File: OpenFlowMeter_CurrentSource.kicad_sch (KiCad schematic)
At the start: 21 parts, among them J1 Screw_Terminal_01x02, Q1 BC856, U1 LT1492

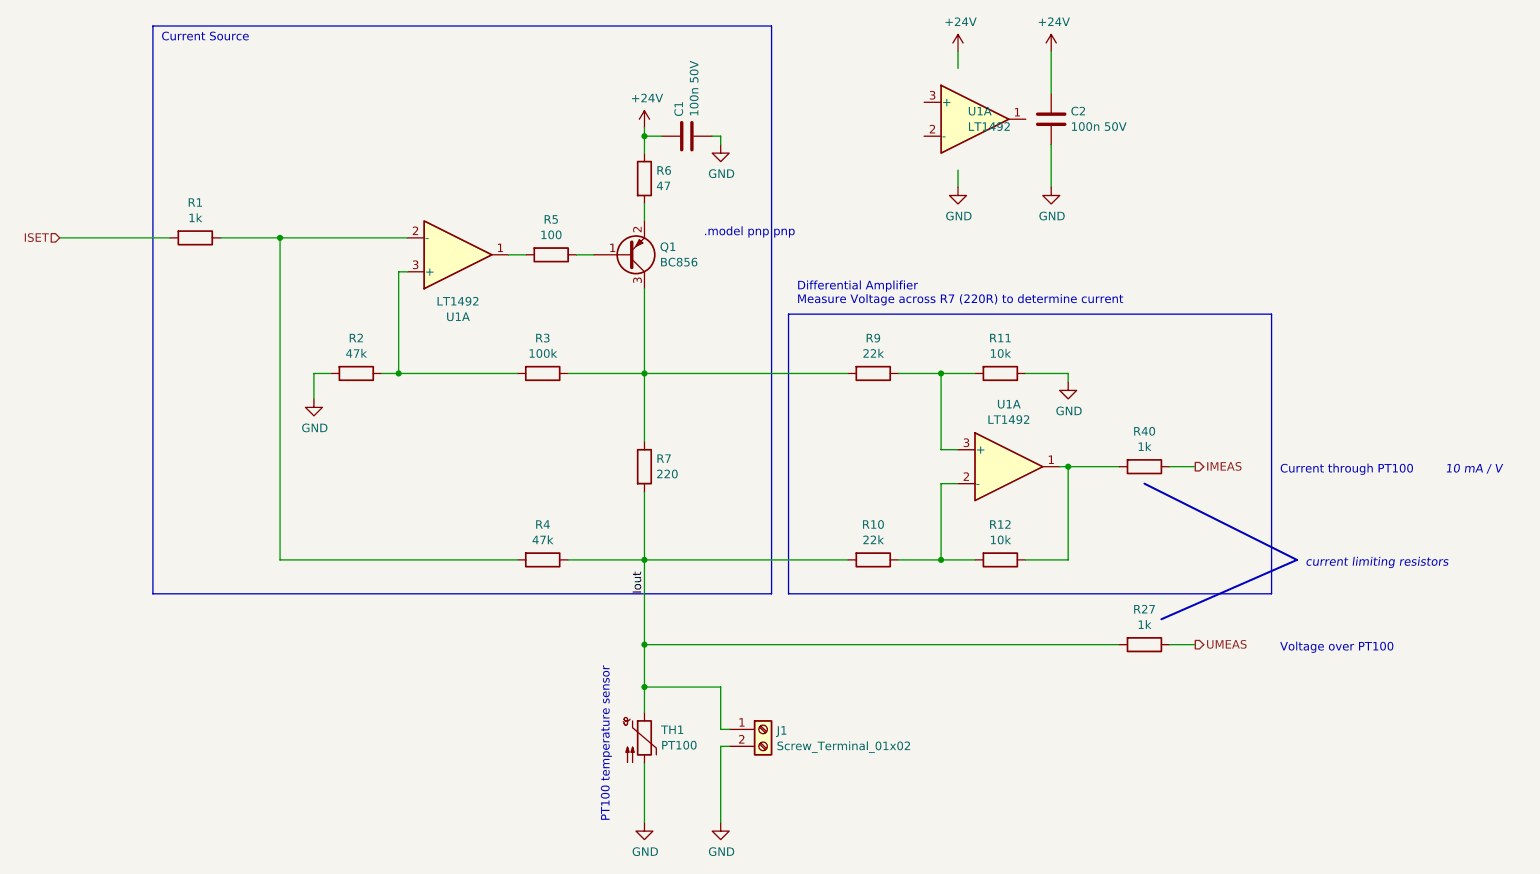
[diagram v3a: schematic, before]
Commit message: implemented changes from tests with the prototype
schematic is updated, layout needs to be done.
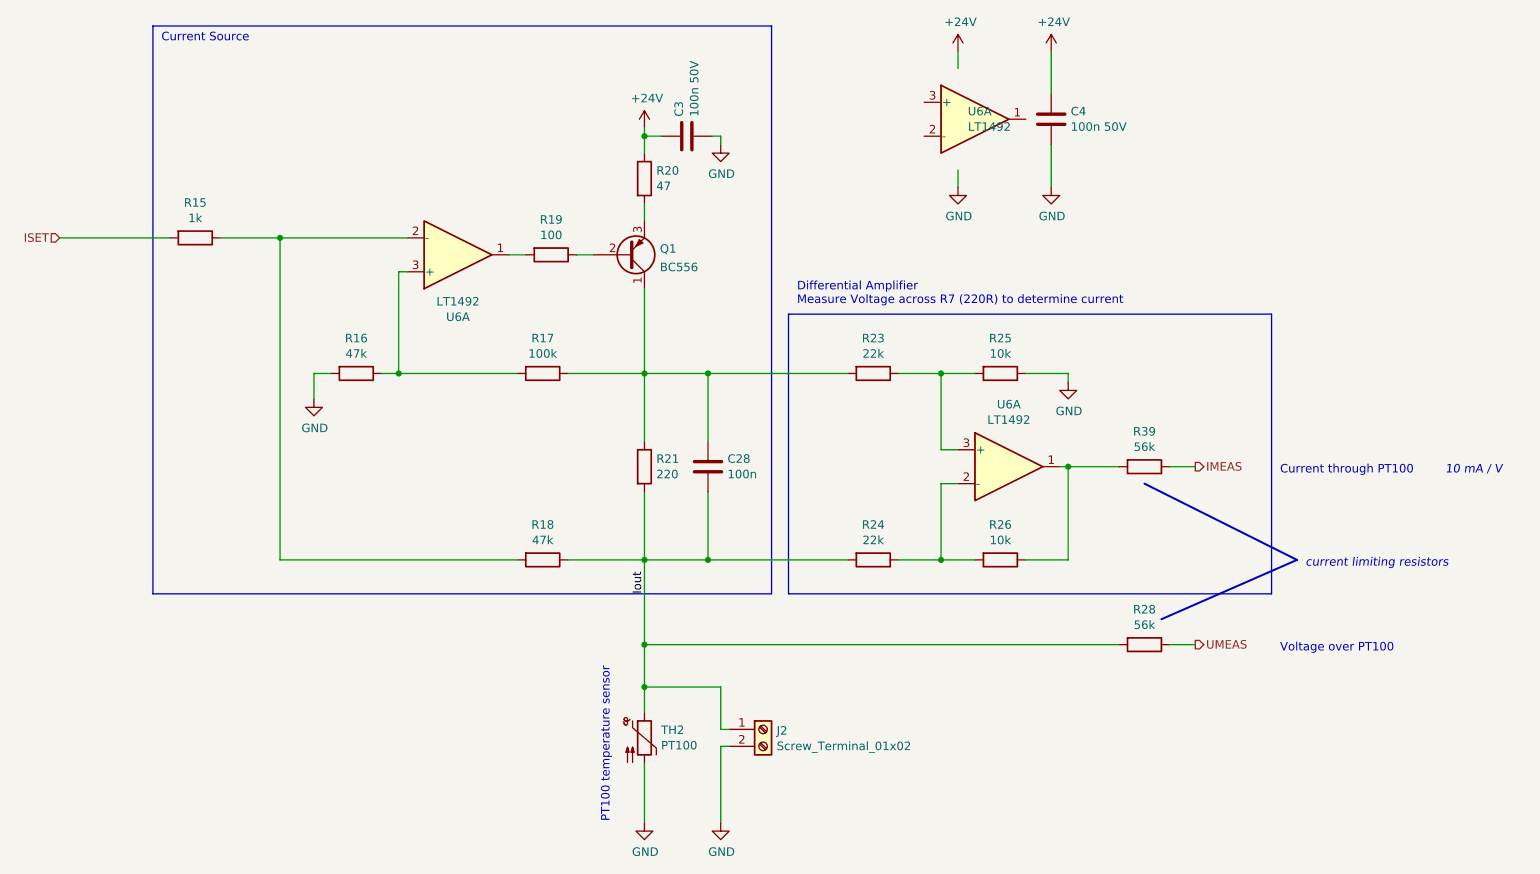
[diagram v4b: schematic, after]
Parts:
- removed Q1: BC856, Package_TO_SOT_SMD:SOT-23, symbol Transistor_BJT:BC856
- added C28: 100n, Capacitor_SMD:C_0603_1608Metric, symbol Device:C
- added Q1: BC556, Package_TO_SOT_THT:TO-92_Inline, symbol Transistor_BJT:BC556
- R28: renamed from R27; value 1k -> 56k
- R39: renamed from R40; value 1k -> 56k
- renumbered C1 to C3, C2 to C4, J1 to J2, R1 to R15, R2 to R16, R3 to R17, R4 to R18, R5 to R19, R6 to R20, R7 to R21, R9 to R23, R10 to R24, R11 to R25, R12 to R26, TH1 to TH2, U1 to U6
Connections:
- net Iout: now also C28.2
- net at R20.2: now also Q1.3 (E)
- net at R19.1: now also Q1.2 (B)
- net at R17.1, R21.1, R23.2: now also C28.1, Q1.1 (C)
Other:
- note removed: ".model pnp pnp"

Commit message: inlcuded switching gain amplifier
aim is to increase the voltage and current reading for small currents and voltages.
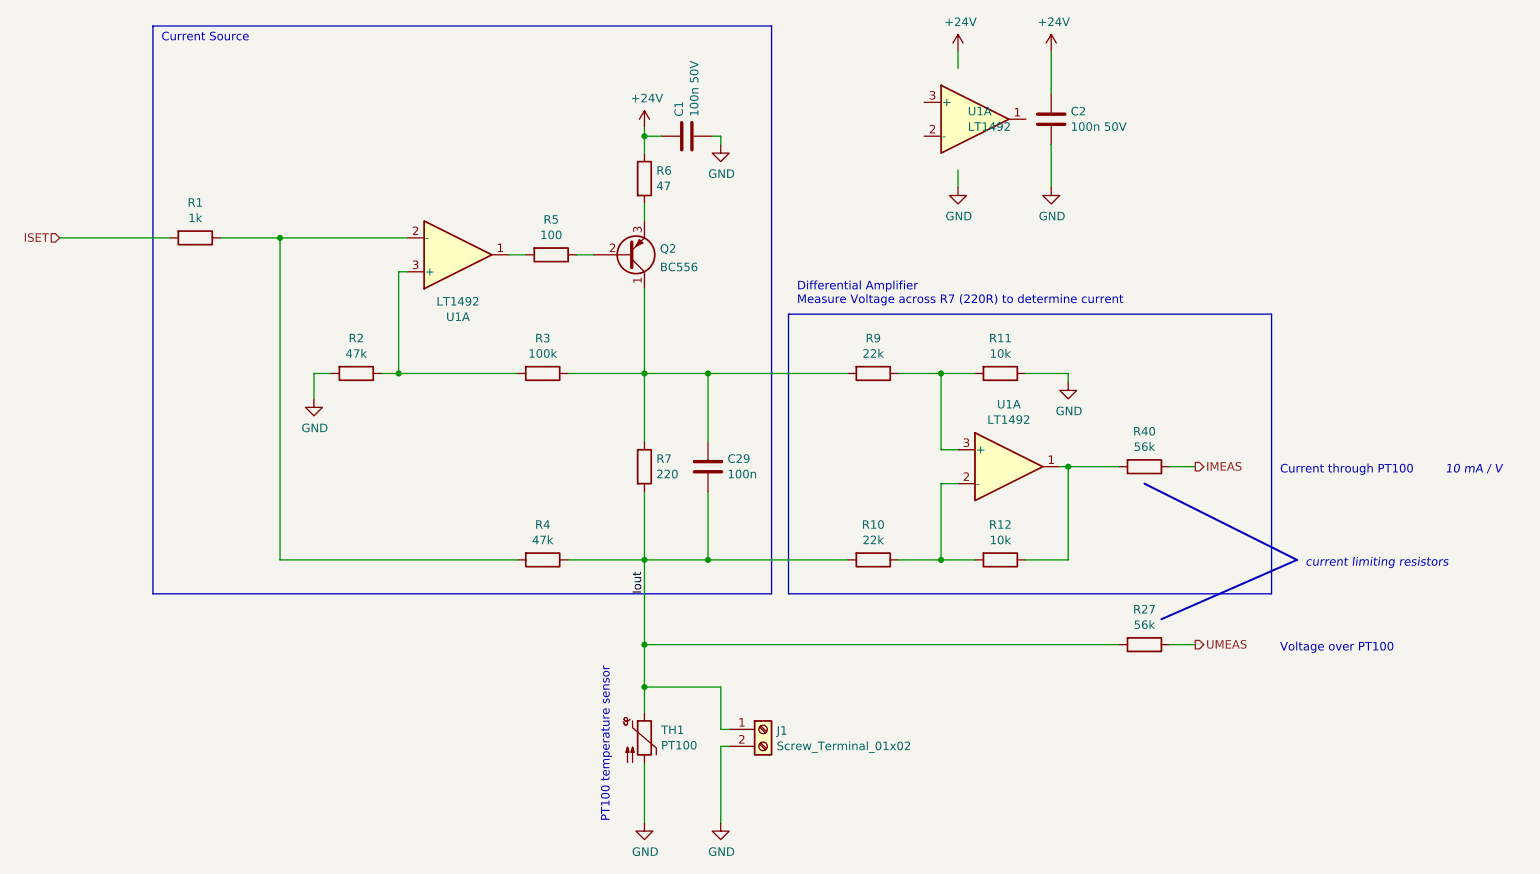
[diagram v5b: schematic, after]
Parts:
- renumbered C3 to C1, C4 to C2, C28 to C29, J2 to J1, Q1 to Q2, R15 to R1, R24 to R10, R25 to R11, R26 to R12, R16 to R2, R28 to R27, R17 to R3, R18 to R4, R39 to R40, R19 to R5, R20 to R6, R21 to R7, R23 to R9, TH2 to TH1, U6 to U1

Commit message: added company to all schematic pages
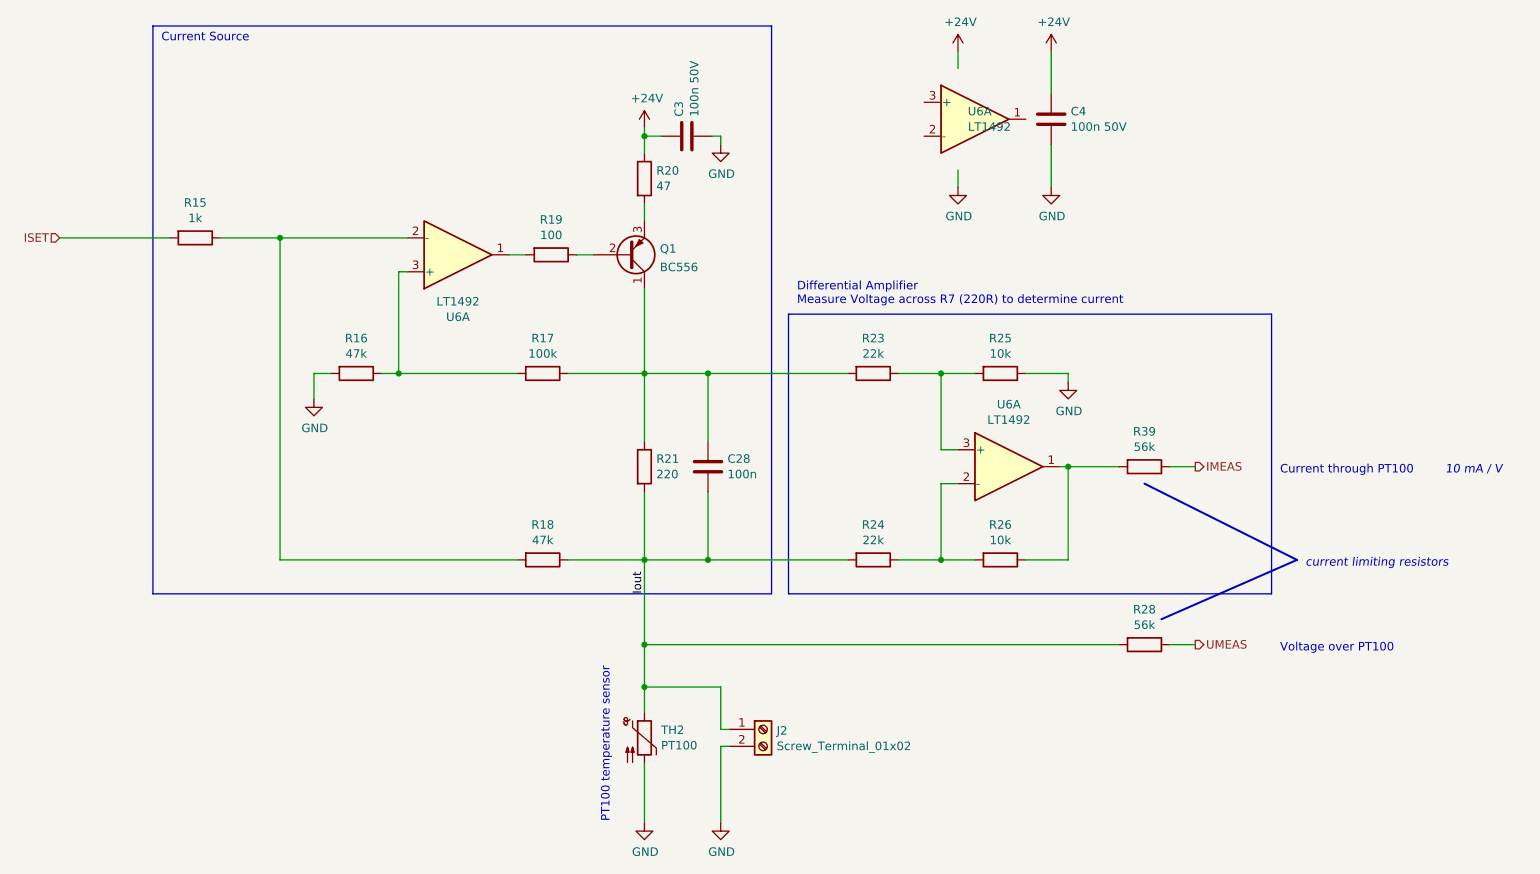
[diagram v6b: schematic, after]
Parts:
- renumbered C29 to C28, C1 to C3, C2 to C4, J1 to J2, Q2 to Q1, R1 to R15, R2 to R16, R3 to R17, R4 to R18, R5 to R19, R6 to R20, R7 to R21, R9 to R23, R10 to R24, R11 to R25, R12 to R26, R27 to R28, R40 to R39, TH1 to TH2, U1 to U6
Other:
- company: (none) -> Jochen Steinmann
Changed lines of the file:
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@@
     (title "Open Flow Meter")
     (date "2021-03-30")
-    (rev "1")
+    (rev "2")
+    (company "Jochen Steinmann")
   )
   (junction (at 181.61 115.57) (diameter 0) (color 0 0 0 0)
@@
   (symbol (lib_id "Amplifier_Operational:LT1492") (at 90.17 83.82 0) (mirror x)
     (in_bom yes) (on_board yes)
-    (property "Reference" "U1" (id 0) (at 90.17 93.1418 0))
+    (property "Reference" "U6" (id 0) (at 90.17 93.1418 0))
     (property "Value" "LT1492" (id 1) (at 90.17 90.8304 0))
     (property "Footprint" "Package_SO:SOIC-8_3.9x4.9mm_P1.27mm" (id 2) (at 90.17 83.82 0)
@@
   (symbol (lib_id "Amplifier_Operational:LT1492") (at 172.72 115.57 0)
     (in_bom yes) (on_board yes)
-    (property "Reference" "U1" (id 0) (at 172.72 106.2482 0))
+    (property "Reference" "U6" (id 0) (at 172.72 106.2482 0))
     (property "Value" "LT1492" (id 1) (at 172.72 108.5596 0))
     (property "Footprint" "Package_SO:SOIC-8_3.9x4.9mm_P1.27mm" (id 2) (at 172.72 115.57 0)
@@
       (effects (font (size 1.27 1.27)) hide)
     )
-    (pin "5")
-    (pin "6")
-    (pin "7")
+    (pin "1")
+    (pin "2")
+    (pin "3")
   )
   (symbol (lib_id "Amplifier_Operational:LT1492") (at 167.64 63.5 0)
     (in_bom yes) (on_board yes)
-    (property "Reference" "U1" (id 0) (at 166.5732 62.3316 0)
+    (property "Reference" "U6" (id 0) (at 166.5732 62.3316 0)
       (effects (font (size 1.27 1.27)) (justify left))
     )
@@
       (effects (font (size 1.27 1.27)) hide)
     )
-    (pin "4")
-    (pin "8")
+    (pin "1")
+    (pin "2")
+    (pin "3")
   )
   (symbol (lib_id "Device:R") (at 50.8 81.28 270)
     (in_bom yes) (on_board yes)
-    (property "Reference" "R1" (id 0) (at 50.8 76.0222 90))
+    (property "Reference" "R15" (id 0) (at 50.8 76.0222 90))
     (property "Value" "1k" (id 1) (at 50.8 78.3336 90))
     (property "Footprint" "Resistor_SMD:R_0603_1608Metric" (id 2) (at 50.8 79.502 90)
@@
   (symbol (lib_id "Device:R") (at 102.87 129.54 270)
     (in_bom yes) (on_board yes)
-    (property "Reference" "R4" (id 0) (at 102.87 124.2822 90))
+    (property "Reference" "R18" (id 0) (at 102.87 124.2822 90))
     (property "Value" "47k" (id 1) (at 102.87 126.5936 90))
     (property "Footprint" "Resistor_SMD:R_0603_1608Metric" (id 2) (at 102.87 127.762 90)
@@
   (symbol (lib_id "Device:R") (at 118.11 72.39 0)
     (in_bom yes) (on_board yes)
-    (property "Reference" "R6" (id 0) (at 119.888 71.2216 0)
+    (property "Reference" "R20" (id 0) (at 119.888 71.2216 0)
       (effects (font (size 1.27 1.27)) (justify left))
     )
@@
   (symbol (lib_id "Device:R") (at 104.14 83.82 270)
     (in_bom yes) (on_board yes)
-    (property "Reference" "R5" (id 0) (at 104.14 78.5622 90))
+    (property "Reference" "R19" (id 0) (at 104.14 78.5622 90))
     (property "Value" "100" (id 1) (at 104.14 80.8736 90))
     (property "Footprint" "Resistor_SMD:R_0603_1608Metric" (id 2) (at 104.14 82.042 90)
@@
   (symbol (lib_id "Device:R") (at 118.11 115.57 0)
     (in_bom yes) (on_board yes)
-    (property "Reference" "R7" (id 0) (at 119.888 114.4016 0)
+    (property "Reference" "R21" (id 0) (at 119.888 114.4016 0)
       (effects (font (size 1.27 1.27)) (justify left))
     )
@@
   (symbol (lib_id "Device:R") (at 102.87 101.6 270)
     (in_bom yes) (on_board yes)
-    (property "Reference" "R3" (id 0) (at 102.87 96.3422 90))
+    (property "Reference" "R17" (id 0) (at 102.87 96.3422 90))
     (property "Value" "100k" (id 1) (at 102.87 98.6536 90))
     (property "Footprint" "Resistor_SMD:R_0603_1608Metric" (id 2) (at 102.87 99.822 90)
@@
   (symbol (lib_id "Device:R") (at 74.93 101.6 270)
     (in_bom yes) (on_board yes)
-    (property "Reference" "R2" (id 0) (at 74.93 96.3422 90))
+    (property "Reference" "R16" (id 0) (at 74.93 96.3422 90))
     (property "Value" "47k" (id 1) (at 74.93 98.6536 90))
     (property "Footprint" "Resistor_SMD:R_0603_1608Metric" (id 2) (at 74.93 99.822 90)
@@
   (symbol (lib_id "Device:R") (at 152.4 101.6 270)
     (in_bom yes) (on_board yes)
-    (property "Reference" "R9" (id 0) (at 152.4 96.3422 90))
+    (property "Reference" "R23" (id 0) (at 152.4 96.3422 90))
     (property "Value" "22k" (id 1) (at 152.4 98.6536 90))
     (property "Footprint" "Resistor_SMD:R_0603_1608Metric" (id 2) (at 152.4 99.822 90)
@@
   (symbol (lib_id "Device:R") (at 152.4 129.54 270)
     (in_bom yes) (on_board yes)
-    (property "Reference" "R10" (id 0) (at 152.4 124.2822 90))
+    (property "Reference" "R24" (id 0) (at 152.4 124.2822 90))
     (property "Value" "22k" (id 1) (at 152.4 126.5936 90))
     (property "Footprint" "Resistor_SMD:R_0603_1608Metric" (id 2) (at 152.4 127.762 90)
@@
   (symbol (lib_id "Device:R") (at 171.45 101.6 270)
     (in_bom yes) (on_board yes)
-    (property "Reference" "R11" (id 0) (at 171.45 96.3422 90))
+    (property "Reference" "R25" (id 0) (at 171.45 96.3422 90))
     (property "Value" "10k" (id 1) (at 171.45 98.6536 90))
     (property "Footprint" "Resistor_SMD:R_0603_1608Metric" (id 2) (at 171.45 99.822 90)
@@
   (symbol (lib_id "Device:R") (at 171.45 129.54 270)
     (in_bom yes) (on_board yes)
-    (property "Reference" "R12" (id 0) (at 171.45 124.2822 90))
+    (property "Reference" "R26" (id 0) (at 171.45 124.2822 90))
     (property "Value" "10k" (id 1) (at 171.45 126.5936 90))
     (property "Footprint" "Resistor_SMD:R_0603_1608Metric" (id 2) (at 171.45 127.762 90)
@@
   (symbol (lib_id "Connector:Screw_Terminal_01x02") (at 135.89 154.94 0)
     (in_bom yes) (on_board yes)
-    (property "Reference" "J1" (id 0) (at 137.922 155.1432 0)
+    (property "Reference" "J2" (id 0) (at 137.922 155.1432 0)
       (effects (font (size 1.27 1.27)) (justify left))
     )
@@
   (symbol (lib_id "Device:R") (at 193.04 142.24 270)
     (in_bom yes) (on_board yes)
-    (property "Reference" "R27" (id 0) (at 193.04 136.9822 90))
+    (property "Reference" "R28" (id 0) (at 193.04 136.9822 90))
     (property "Value" "56k" (id 1) (at 193.04 139.2936 90))
     (property "Footprint" "Resistor_SMD:R_0603_1608Metric" (id 2) (at 193.04 140.462 90)
@@
   (symbol (lib_id "Sensor_Temperature:PT100") (at 118.11 156.21 0)
     (in_bom yes) (on_board yes)
-    (property "Reference" "TH1" (id 0) (at 120.5992 155.0416 0)
+    (property "Reference" "TH2" (id 0) (at 120.5992 155.0416 0)
       (effects (font (size 1.27 1.27)) (justify left))
     )
@@
   (symbol (lib_id "Device:C") (at 179.07 63.5 0)
     (in_bom yes) (on_board yes)
-    (property "Reference" "C2" (id 0) (at 181.991 62.3316 0)
+    (property "Reference" "C4" (id 0) (at 181.991 62.3316 0)
       (effects (font (size 1.27 1.27)) (justify left))
     )
@@
   (symbol (lib_id "Device:C") (at 124.46 66.04 90)
     (in_bom yes) (on_board yes)
-    (property "Reference" "C1" (id 0) (at 123.2916 63.119 0)
+    (property "Reference" "C3" (id 0) (at 123.2916 63.119 0)
       (effects (font (size 1.27 1.27)) (justify left))
     )
@@
   (symbol (lib_id "Device:R") (at 193.04 115.57 270)
     (in_bom yes) (on_board yes)
-    (property "Reference" "R40" (id 0) (at 193.04 110.3122 90))
+    (property "Reference" "R39" (id 0) (at 193.04 110.3122 90))
     (property "Value" "56k" (id 1) (at 193.04 112.6236 90))
     (property "Footprint" "Resistor_SMD:R_0603_1608Metric" (id 2) (at 193.04 113.792 90)
@@
   (symbol (lib_id "Transistor_BJT:BC556") (at 115.57 83.82 0) (mirror x)
     (in_bom yes) (on_board yes) (fields_autoplaced)
-    (property "Reference" "Q2" (id 0) (at 120.4214 82.9115 0)
+    (property "Reference" "Q1" (id 0) (at 120.4214 82.9115 0)
       (effects (font (size 1.27 1.27)) (justify left))
     )
@@
   (symbol (lib_id "Device:C") (at 127.635 115.57 0)
     (in_bom yes) (on_board yes)
-    (property "Reference" "C29" (id 0) (at 130.556 114.4016 0)
-      (effects (font (size 1.27 1.27)) (justify left))
-    )
+    (property "Reference" "C28" (id 0) (at 130.556 114.4016 0)
+      (effects (font (size 1.27 1.27)) (justify left))
+    )
